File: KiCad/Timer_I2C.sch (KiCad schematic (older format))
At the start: 7 parts

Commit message: 24/05
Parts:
- R_MFP: renamed from 10k; value R_US -> 10k
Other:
- moved on the sheet: R_MFP
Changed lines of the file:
@@
 $Descr A4 11693 8268
 encoding utf-8
-Sheet 2 6
+Sheet 6 6
 Title ""
 Date ""
@@
 Vcc_5v
 $Comp
-L power:GNDREF #PWR?
+L power:GNDREF #PWR0118
 U 1 1 60A51684
 P 4200 3650
-F 0 "#PWR?" H 4200 3400 50  0001 C CNN
+F 0 "#PWR0118" H 4200 3400 50  0001 C CNN
 F 1 "GNDREF" H 4205 3477 50  0000 C CNN
 F 2 "" H 4200 3650 50  0001 C CNN
@@
 	4200 3400 4200 3650
 $Comp
-L power:GNDREF #PWR?
+L power:GNDREF #PWR0119
 U 1 1 60A525BC
 P 4600 2500
-F 0 "#PWR?" H 4600 2250 50  0001 C CNN
+F 0 "#PWR0119" H 4600 2250 50  0001 C CNN
 F 1 "GNDREF" H 4605 2327 50  0000 C CNN
 F 2 "" H 4600 2500 50  0001 C CNN
@@
 Text HLabel 3050 3100 0    50   BiDi ~ 0
 Multifunction_pin
-Text GLabel 3300 3400 0    50   Input ~ 0
+Text GLabel 3250 3400 0    50   Input ~ 0
 Vcc_5v
 $Comp
-L Device:R_US 10k
+L Device:R_US R_MFP
 U 1 1 60A57A7B
-P 3600 3250
-F 0 "10k" H 3668 3296 50  0000 L CNN
-F 1 "R_US" H 3668 3205 50  0000 L CNN
-F 2 "" V 3640 3240 50  0001 C CNN
-F 3 "~" H 3600 3250 50  0001 C CNN
-	1    3600 3250
-	1    0    0    -1
-$EndComp
-Wire Wire Line
-	3300 3400 3600 3400
-Wire Wire Line
-	3600 3100 3800 3100
+P 3550 3250
+F 0 "R_MFP" H 3618 3296 50  0000 L CNN
+F 1 "10k" H 3618 3205 50  0000 L CNN
+F 2 "" V 3590 3240 50  0001 C CNN
+F 3 "~" H 3550 3250 50  0001 C CNN
+	1    3550 3250
+	1    0    0    -1
+$EndComp
+Wire Wire Line
+	3250 3400 3550 3400
 Wire Wire Line
 	3750 2900 3800 2900
@@
 Connection ~ 3750 2900
 Wire Wire Line
-	3050 3100 3600 3100
-Connection ~ 3600 3100
+	3050 3100 3550 3100
 Connection ~ 3400 2400
 Connection ~ 3400 2800
@@
 	6800 3500 5550 3500
 $Comp
-L power:GNDREF #PWR?
+L power:GNDREF #PWR0120
 U 1 1 60A784D6
 P 5550 3500
-F 0 "#PWR?" H 5550 3250 50  0001 C CNN
+F 0 "#PWR0120" H 5550 3250 50  0001 C CNN
 F 1 "GNDREF" H 5555 3327 50  0000 C CNN
 F 2 "" H 5550 3500 50  0001 C CNN
@@
 Wire Wire Line
 	4300 2500 4600 2500
+Connection ~ 3550 3100
+Wire Wire Line
+	3550 3100 3800 3100
 $EndSCHEMATC

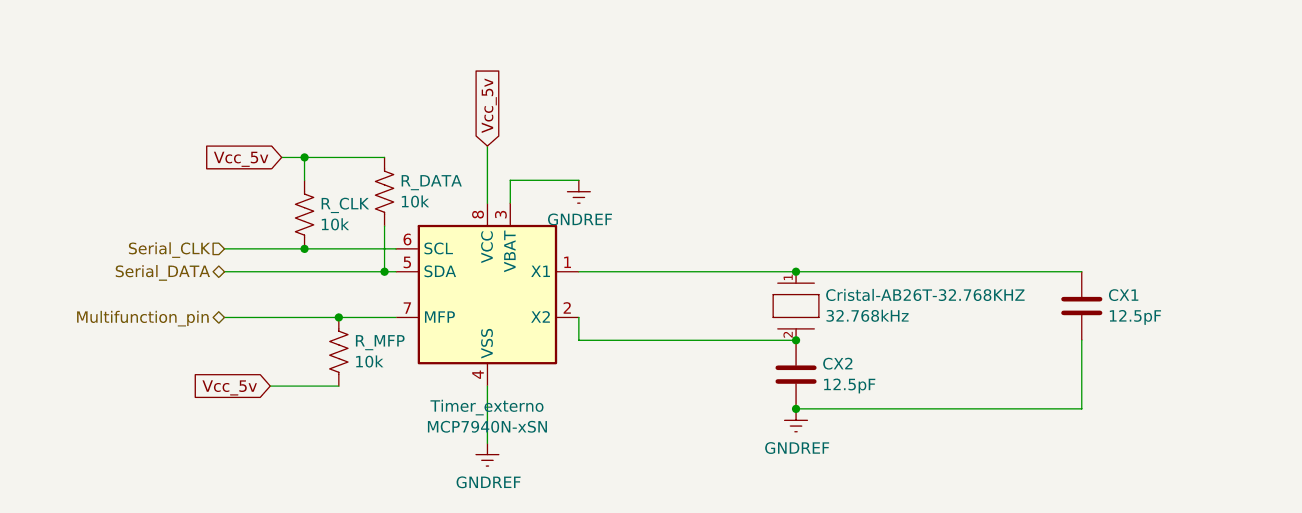
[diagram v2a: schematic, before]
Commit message: PWM and minor changes
Filtro Butterworth e conexão dos LED's
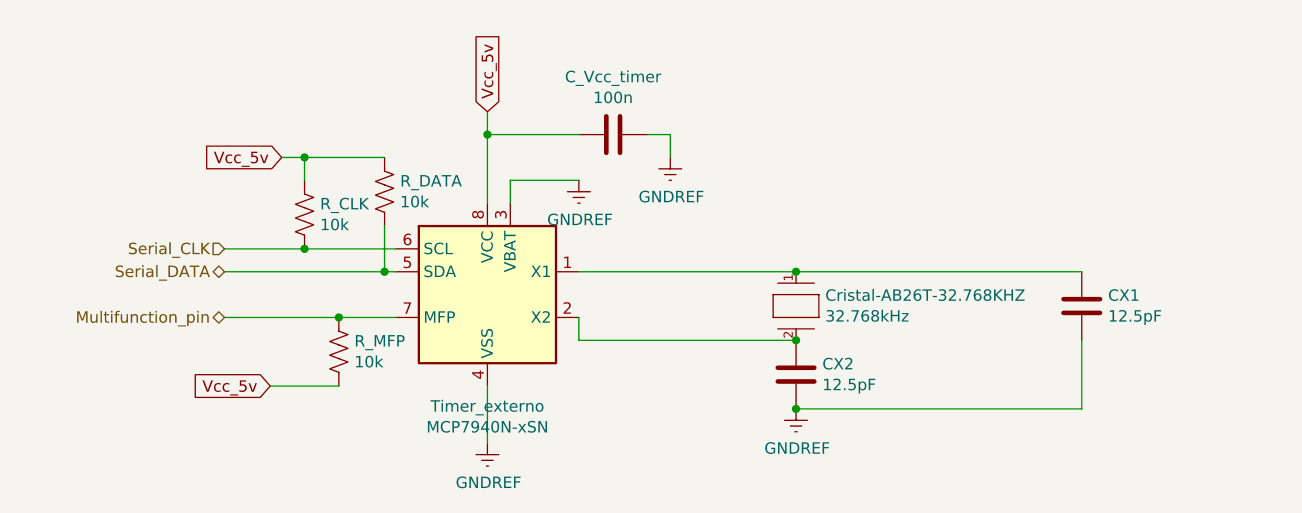
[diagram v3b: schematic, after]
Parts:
- added C_Vcc_timer: 100n, symbol Device:C
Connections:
- net GNDREF: now also C_Vcc_timer.1
- net Vcc_5v: now also C_Vcc_timer.2
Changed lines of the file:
@@
 $Descr A4 11693 8268
 encoding utf-8
-Sheet 6 8
+Sheet 6 9
 Title ""
 Date ""
@@
 Comment4 ""
 $EndDescr
-Text GLabel 4200 2350 1    50   Input ~ 0
+Text GLabel 4200 2200 1    50   Input ~ 0
 Vcc_5v
 $Comp
@@
 Connection ~ 5550 3200
 Wire Wire Line
-	4200 2350 4200 2600
-Wire Wire Line
 	4300 2500 4600 2500
 Connection ~ 3550 3100
 Wire Wire Line
 	3550 3100 3800 3100
+Wire Wire Line
+	4200 2200 4200 2300
+Wire Wire Line
+	4200 2300 4600 2300
+Connection ~ 4200 2300
+Wire Wire Line
+	4200 2300 4200 2600
+$Comp
+L Device:C C_Vcc_timer
+U 1 1 60B2356F
+P 4750 2300
+F 0 "C_Vcc_timer" V 4498 2300 50  0000 C CNN
+F 1 "100n" V 4589 2300 50  0000 C CNN
+F 2 "" H 4788 2150 50  0001 C CNN
+F 3 "~" H 4750 2300 50  0001 C CNN
+	1    4750 2300
+	0    1    1    0
+$EndComp
+$Comp
+L power:GNDREF #PWR?
+U 1 1 60B242E7
+P 5000 2400
+F 0 "#PWR?" H 5000 2150 50  0001 C CNN
+F 1 "GNDREF" H 5005 2227 50  0000 C CNN
+F 2 "" H 5000 2400 50  0001 C CNN
+F 3 "" H 5000 2400 50  0001 C CNN
+	1    5000 2400
+	1    0    0    -1
+$EndComp
+Wire Wire Line
+	4900 2300 5000 2300
+Wire Wire Line
+	5000 2300 5000 2400
 $EndSCHEMATC

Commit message: v1_final
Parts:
- renumbered C_Vcc_timer to C_Vcc_timer1, Cristal-AB26T-32.768KHZ to Cristal-AB26T-32.768KHZ1, R_CLK to R_CLK1, R_DATA to R_DATA1, R_MFP to R_MFP1, Timer_externo to Timer_externo1
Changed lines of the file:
@@
 Vcc_5v
 $Comp
-L Device:R_US R_CLK
+L Device:R_US R_CLK1
 U 1 1 60A54E37
 P 3400 2650
-F 0 "R_CLK" H 3468 2696 50  0000 L CNN
+F 0 "R_CLK1" H 3468 2696 50  0000 L CNN
 F 1 "10k" H 3468 2605 50  0000 L CNN
 F 2 "" V 3440 2640 50  0001 C CNN
@@
 	3400 2400 3400 2500
 $Comp
-L Timer:MCP7940N-xSN Timer_externo
+L Timer:MCP7940N-xSN Timer_externo1
 U 1 1 60A50A9A
 P 4200 3000
-F 0 "Timer_externo" H 4200 2511 50  0000 C CNN
+F 0 "Timer_externo1" H 4200 2511 50  0000 C CNN
 F 1 "MCP7940N-xSN" H 4200 2420 50  0000 C CNN
 F 2 "" H 4200 3000 50  0001 C CNN
@@
 Vcc_5v
 $Comp
-L Device:R_US R_MFP
+L Device:R_US R_MFP1
 U 1 1 60A57A7B
 P 3550 3250
-F 0 "R_MFP" H 3618 3296 50  0000 L CNN
+F 0 "R_MFP1" H 3618 3296 50  0000 L CNN
 F 1 "10k" H 3618 3205 50  0000 L CNN
 F 2 "" V 3590 3240 50  0001 C CNN
@@
 	3750 2700 3750 2900
 $Comp
-L Device:R_US R_DATA
+L Device:R_US R_DATA1
 U 1 1 60A55734
 P 3750 2550
-F 0 "R_DATA" H 3818 2596 50  0000 L CNN
+F 0 "R_DATA1" H 3818 2596 50  0000 L CNN
 F 1 "10k" H 3818 2505 50  0000 L CNN
 F 2 "" V 3790 2540 50  0001 C CNN
@@
 Connection ~ 5550 3500
 $Comp
-L My_Lib:AB26T-32.768KHZ Cristal-AB26T-32.768KHZ
+L My_Lib:AB26T-32.768KHZ Cristal-AB26T-32.768KHZ1
 U 1 1 60A5D7A4
 P 5550 2900
-F 0 "Cristal-AB26T-32.768KHZ" V 5654 3028 50  0000 L CNN
+F 0 "Cristal-AB26T-32.768KHZ1" V 5654 3028 50  0000 L CNN
 F 1 "32.768kHz" V 5745 3028 50  0000 L CNN
 F 2 "Abracon-AB26T-32.768KHZ-*" H 5550 3300 50  0001 L CNN
@@
 	4200 2300 4200 2600
 $Comp
-L Device:C C_Vcc_timer
+L Device:C C_Vcc_timer1
 U 1 1 60B2356F
 P 4750 2300
-F 0 "C_Vcc_timer" V 4498 2300 50  0000 C CNN
+F 0 "C_Vcc_timer1" V 4498 2300 50  0000 C CNN
 F 1 "100n" V 4589 2300 50  0000 C CNN
 F 2 "" H 4788 2150 50  0001 C CNN
@@
 $EndComp
 $Comp
-L power:GNDREF #PWR?
+L power:GNDREF #PWR0125
 U 1 1 60B242E7
 P 5000 2400
-F 0 "#PWR?" H 5000 2150 50  0001 C CNN
+F 0 "#PWR0125" H 5000 2150 50  0001 C CNN
 F 1 "GNDREF" H 5005 2227 50  0000 C CNN
 F 2 "" H 5000 2400 50  0001 C CNN

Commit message: adição departe dos footprints
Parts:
- Cristal-AB26T-32.768KHZ1: footprint Abracon-AB26T-32.768KHZ-* -> (none)
- R_CLK1, R_DATA1, R_MFP1: footprint (none) -> Resistor_SMD:R_0805_2012Metric
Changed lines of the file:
@@
 $Descr A4 11693 8268
 encoding utf-8
-Sheet 6 9
+Sheet 4 10
 Title ""
 Date ""
@@
 F 0 "R_CLK1" H 3468 2696 50  0000 L CNN
 F 1 "10k" H 3468 2605 50  0000 L CNN
-F 2 "" V 3440 2640 50  0001 C CNN
+F 2 "Resistor_SMD:R_0805_2012Metric" V 3440 2640 50  0001 C CNN
 F 3 "~" H 3400 2650 50  0001 C CNN
 	1    3400 2650
@@
 F 0 "R_MFP1" H 3618 3296 50  0000 L CNN
 F 1 "10k" H 3618 3205 50  0000 L CNN
-F 2 "" V 3590 3240 50  0001 C CNN
+F 2 "Resistor_SMD:R_0805_2012Metric" V 3590 3240 50  0001 C CNN
 F 3 "~" H 3550 3250 50  0001 C CNN
 	1    3550 3250
@@
 F 0 "R_DATA1" H 3818 2596 50  0000 L CNN
 F 1 "10k" H 3818 2505 50  0000 L CNN
-F 2 "" V 3790 2540 50  0001 C CNN
+F 2 "Resistor_SMD:R_0805_2012Metric" V 3790 2540 50  0001 C CNN
 F 3 "~" H 3750 2550 50  0001 C CNN
 	1    3750 2550
@@
 F 0 "Cristal-AB26T-32.768KHZ1" V 5654 3028 50  0000 L CNN
 F 1 "32.768kHz" V 5745 3028 50  0000 L CNN
-F 2 "Abracon-AB26T-32.768KHZ-*" H 5550 3300 50  0001 L CNN
+F 2 "" H 5550 3300 50  0001 L CNN
 F 3 "https://upverter.com/datasheet/e60e0d8762f6cc85b53388b76005bd605569ec5b.pdf" H 5550 3400 50  0001 L CNN
 F 4 "±20ppm" H 5550 3500 50  0001 L CNN "Frequency Tolerance"

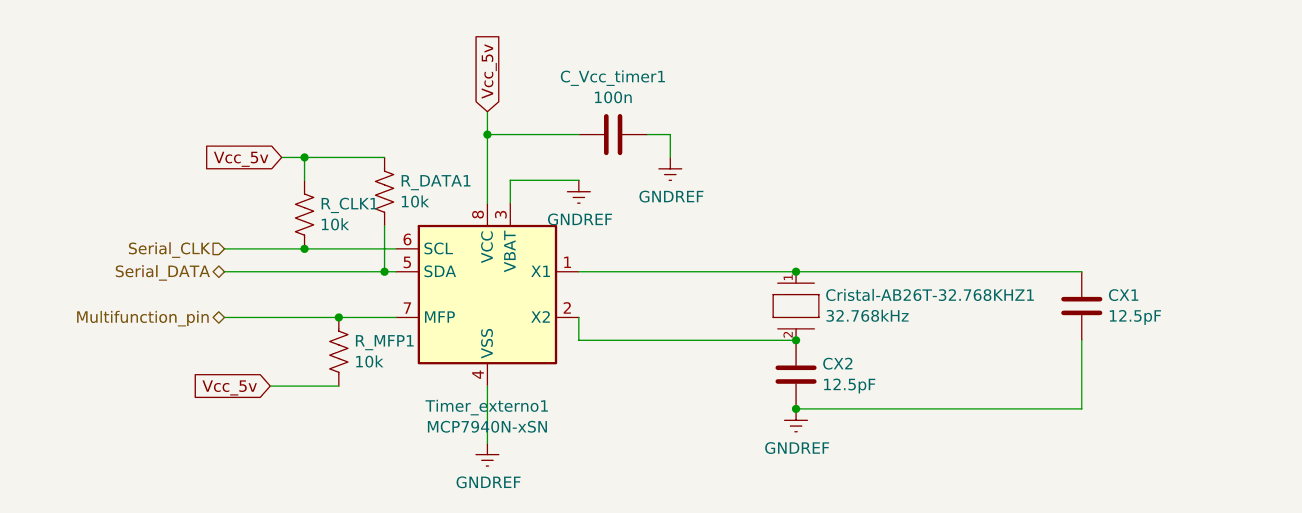
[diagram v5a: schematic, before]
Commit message: adição de mais footprints
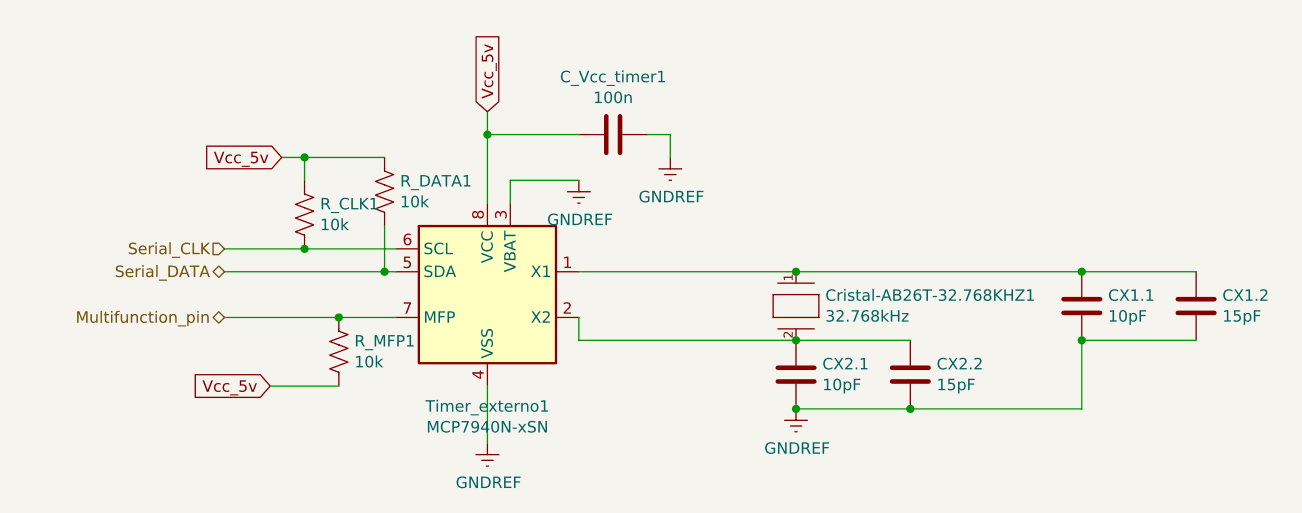
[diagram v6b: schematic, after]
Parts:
- added CX1.2, CX2.2: 15pF, Capacitor_SMD:C_0805_2012Metric_Pad1.18x1.45mm_HandSolder, symbol Device:C
- CX1.1: renamed from CX1; value 12.5pF -> 10pF; footprint (none) -> Capacitor_SMD:C_0805_2012Metric_Pad1.18x1.45mm_HandSolder
- CX2.1: renamed from CX2; value 12.5pF -> 10pF; footprint (none) -> Capacitor_SMD:C_0805_2012Metric_Pad1.18x1.45mm_HandSolder
- C_Vcc_timer1: footprint (none) -> Capacitor_SMD:C_0805_2012Metric_Pad1.18x1.45mm_HandSolder
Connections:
- net GNDREF: now also CX1.2.2, CX2.2.2
- net at CX1.1.1, Cristal-AB26T-32.768KHZ1.1, Timer_externo1.1 (X1): now also CX1.2.1
- net at CX2.1.2, Cristal-AB26T-32.768KHZ1.2, Timer_externo1.2 (X2): now also CX2.2.1
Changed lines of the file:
@@
 	4600 3200 5550 3200
 $Comp
-L Device:C CX1
+L Device:C CX1.1
 U 1 1 60A761D7
 P 6800 3050
-F 0 "CX1" H 6915 3096 50  0000 L CNN
-F 1 "12.5pF" H 6915 3005 50  0000 L CNN
-F 2 "" H 6838 2900 50  0001 C CNN
+F 0 "CX1.1" H 6915 3096 50  0000 L CNN
+F 1 "10pF" H 6915 3005 50  0000 L CNN
+F 2 "Capacitor_SMD:C_0805_2012Metric_Pad1.18x1.45mm_HandSolder" H 6838 2900 50  0001 C CNN
 F 3 "~" H 6800 3050 50  0001 C CNN
 	1    6800 3050
@@
 $EndComp
 $Comp
-L Device:C CX2
+L Device:C CX2.1
 U 1 1 60A779E3
 P 5550 3350
-F 0 "CX2" H 5435 3304 50  0000 R CNN
-F 1 "12.5pF" H 5435 3395 50  0000 R CNN
-F 2 "" H 5588 3200 50  0001 C CNN
+F 0 "CX2.1" H 5435 3304 50  0000 R CNN
+F 1 "10pF" H 5435 3395 50  0000 R CNN
+F 2 "Capacitor_SMD:C_0805_2012Metric_Pad1.18x1.45mm_HandSolder" H 5588 3200 50  0001 C CNN
 F 3 "~" H 5550 3350 50  0001 C CNN
 	1    5550 3350
@@
 Wire Wire Line
 	6800 3200 6800 3500
-Wire Wire Line
-	6800 3500 5550 3500
 $Comp
 L power:GNDREF #PWR0120
@@
 F 0 "C_Vcc_timer1" V 4498 2300 50  0000 C CNN
 F 1 "100n" V 4589 2300 50  0000 C CNN
-F 2 "" H 4788 2150 50  0001 C CNN
+F 2 "Capacitor_SMD:C_0805_2012Metric_Pad1.18x1.45mm_HandSolder" H 4788 2150 50  0001 C CNN
 F 3 "~" H 4750 2300 50  0001 C CNN
 	1    4750 2300
@@
 Wire Wire Line
 	5000 2300 5000 2400
+$Comp
+L Device:C CX1.2
+U 1 1 60E74486
+P 7300 3050
+F 0 "CX1.2" H 7415 3096 50  0000 L CNN
+F 1 "15pF" H 7415 3005 50  0000 L CNN
+F 2 "Capacitor_SMD:C_0805_2012Metric_Pad1.18x1.45mm_HandSolder" H 7338 2900 50  0001 C CNN
+F 3 "~" H 7300 3050 50  0001 C CNN
+	1    7300 3050
+	1    0    0    -1
+$EndComp
+$Comp
+L Device:C CX2.2
+U 1 1 60E74B05
+P 6050 3350
+F 0 "CX2.2" H 6165 3396 50  0000 L CNN
+F 1 "15pF" H 6165 3305 50  0000 L CNN
+F 2 "Capacitor_SMD:C_0805_2012Metric_Pad1.18x1.45mm_HandSolder" H 6088 3200 50  0001 C CNN
+F 3 "~" H 6050 3350 50  0001 C CNN
+	1    6050 3350
+	1    0    0    -1
+$EndComp
+Wire Wire Line
+	5550 3500 6050 3500
+Connection ~ 6050 3500
+Wire Wire Line
+	6050 3500 6800 3500
+Wire Wire Line
+	6050 3200 5550 3200
+Wire Wire Line
+	6800 2900 7300 2900
+Connection ~ 6800 2900
+Wire Wire Line
+	7300 3200 6800 3200
+Connection ~ 6800 3200
 $EndSCHEMATC

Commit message: pble_zip
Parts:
- Cristal-AB26T-32.768KHZ1: footprint (none) -> Crystal:Crystal_Round_D3.0mm_Vertical
- Timer_externo1: footprint (none) -> Package_SO:SOIC-8_3.9x4.9mm_P1.27mm
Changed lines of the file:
@@
 F 0 "Timer_externo1" H 4200 2511 50  0000 C CNN
 F 1 "MCP7940N-xSN" H 4200 2420 50  0000 C CNN
-F 2 "" H 4200 3000 50  0001 C CNN
+F 2 "Package_SO:SOIC-8_3.9x4.9mm_P1.27mm" H 4200 3000 50  0001 C CNN
 F 3 "http://ww1.microchip.com/downloads/en/DeviceDoc/20005010F.pdf" H 4200 3000 50  0001 C CNN
 	1    4200 3000
@@
 F 0 "Cristal-AB26T-32.768KHZ1" V 5654 3028 50  0000 L CNN
 F 1 "32.768kHz" V 5745 3028 50  0000 L CNN
-F 2 "" H 5550 3300 50  0001 L CNN
+F 2 "Crystal:Crystal_Round_D3.0mm_Vertical" H 5550 3300 50  0001 L CNN
 F 3 "https://upverter.com/datasheet/e60e0d8762f6cc85b53388b76005bd605569ec5b.pdf" H 5550 3400 50  0001 L CNN
 F 4 "±20ppm" H 5550 3500 50  0001 L CNN "Frequency Tolerance"

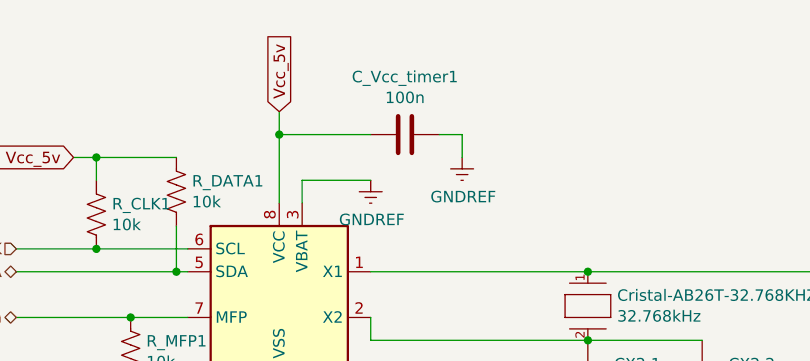
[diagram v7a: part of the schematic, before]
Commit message: correção P1: LCD e Capacitores
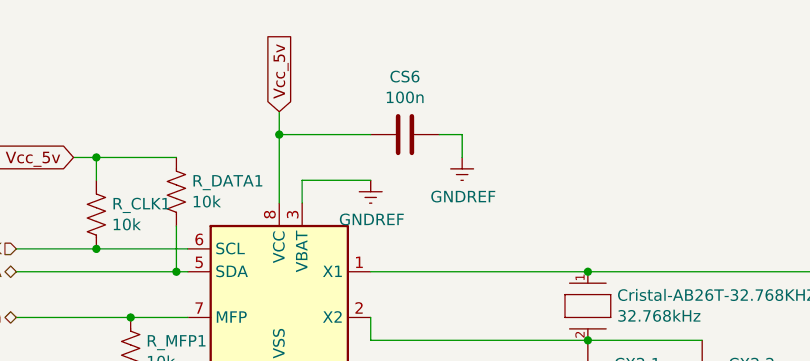
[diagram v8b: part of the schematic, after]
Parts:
- renumbered C_Vcc_timer1 to CS6
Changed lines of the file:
@@
 	4200 2300 4200 2600
 $Comp
-L Device:C C_Vcc_timer1
+L Device:C CS6
 U 1 1 60B2356F
 P 4750 2300
-F 0 "C_Vcc_timer1" V 4498 2300 50  0000 C CNN
+F 0 "CS6" V 4498 2300 50  0000 C CNN
 F 1 "100n" V 4589 2300 50  0000 C CNN
 F 2 "Capacitor_SMD:C_0805_2012Metric_Pad1.18x1.45mm_HandSolder" H 4788 2150 50  0001 C CNN
